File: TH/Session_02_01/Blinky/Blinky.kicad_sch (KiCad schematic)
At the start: 12 parts, among them SW1 SW_SPDT, U1 TLC551CD‎

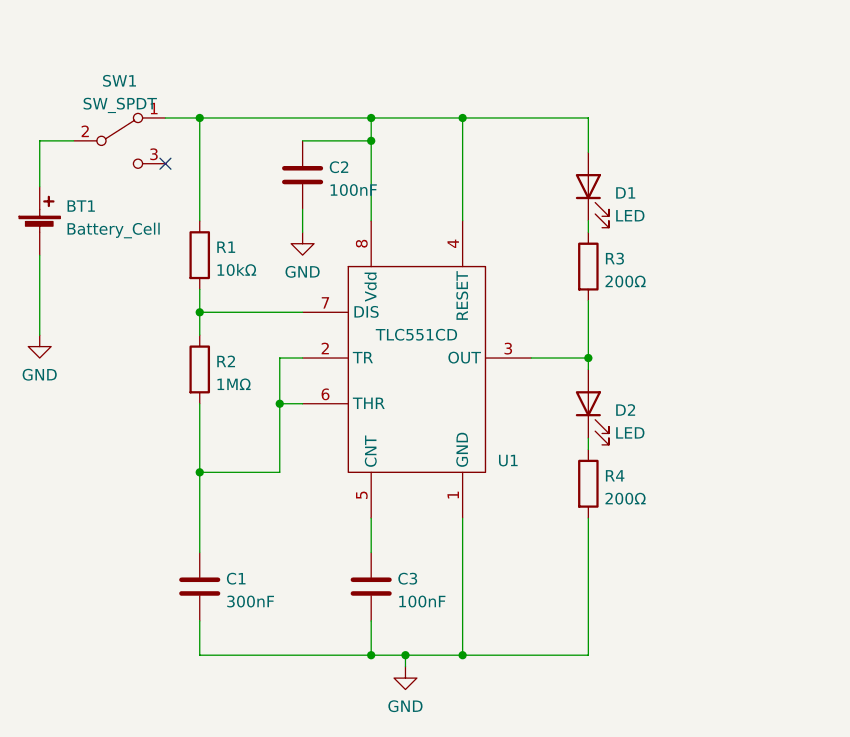
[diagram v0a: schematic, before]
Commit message: Revamps the through-hole project as transistor based
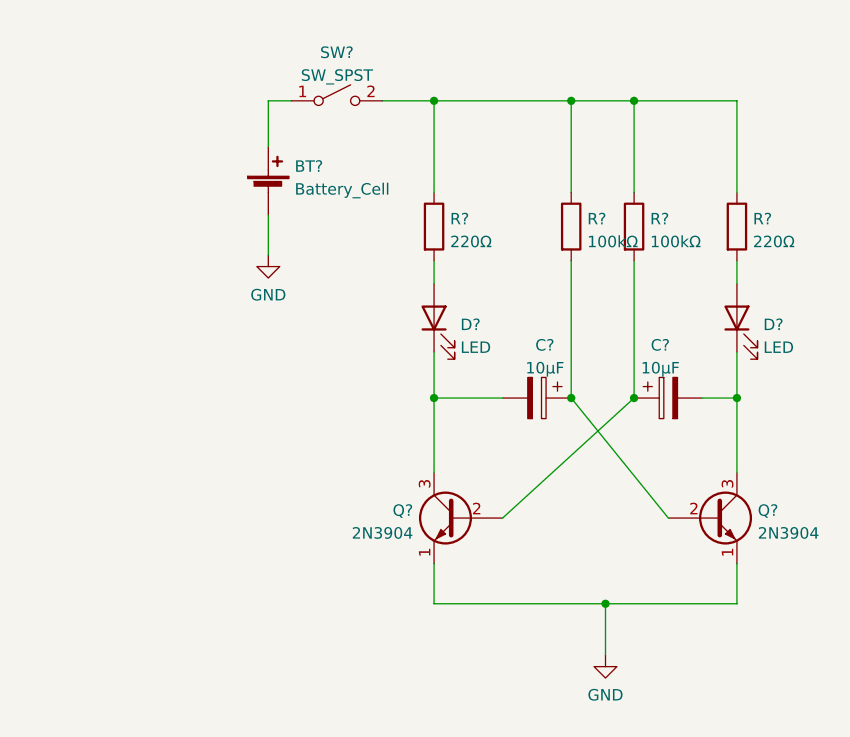
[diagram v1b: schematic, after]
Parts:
- removed BT1: Battery_Cell, Battery:BatteryHolder_Keystone_3000_1x12mm, symbol Device:Battery_Cell
- removed C1: 300nF, Capacitor_THT:C_Disc_D5.0mm_W2.5mm_P5.00mm, symbol Device:C
- removed C2, C3: 100nF, Capacitor_THT:C_Disc_D5.0mm_W2.5mm_P5.00mm, symbol Device:C
- removed D1, D2: LED, LED_THT:LED_D5.0mm, symbol Device:LED
- removed R1: 10kΩ, Resistor_THT:R_Axial_DIN0207_L6.3mm_D2.5mm_P10.16mm_Horizontal, symbol Device:R
- removed R2: 1MΩ, Resistor_THT:R_Axial_DIN0207_L6.3mm_D2.5mm_P10.16mm_Horizontal, symbol Device:R
- removed R3, R4: 200Ω, Resistor_THT:R_Axial_DIN0207_L6.3mm_D2.5mm_P10.16mm_Horizontal, symbol Device:R
- removed SW1: SW_SPDT, Blinky_ZAM:SSK-1202, symbol Switch:SW_SPDT
- removed U1: TLC551CD‎, Package_DIP:DIP-8_W7.62mm_Socket, symbol Blinky:TLC551CD‎
- added BT?: Battery_Cell, Battery:BatteryHolder_Keystone_3000_1x12mm, symbol Device:Battery_Cell
- added C? (x2): 10μF, Capacitor_THT:CP_Radial_D5.0mm_P2.50mm, symbol Device:C_Polarized
- added D? (x2): LED, LED_THT:LED_D5.0mm, symbol Device:LED
- added Q? (x2): 2N3904, Package_TO_SOT_THT:TO-92_Inline, symbol Transistor_BJT:2N3904
- added R? (x2): 220Ω, Resistor_THT:R_Axial_DIN0207_L6.3mm_D2.5mm_P2.54mm_Vertical, symbol Device:R
- added R? (x2): 100kΩ, Resistor_THT:R_Axial_DIN0207_L6.3mm_D2.5mm_P2.54mm_Vertical, symbol Device:R
- added SW?: SW_SPST, Blinky_ZAM:SSK-1202, symbol Switch:SW_SPST
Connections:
- net GND: now also BT?.2 (-), Q?.1 (E), Q?.1 (E)
- new net: C?.2, D?.1 (K), Q?.3 (C) (x2)
- new net: D?.2 (A), R?.2 (x2)
- new net: R?.1, R?.1, R?.1, R?.1, SW?.2 (B)
- new net: C?.1, Q?.2 (B), R?.2 (x2)
- new net: BT?.1 (+), SW?.1 (A)
- no-connect marks 1 -> 0

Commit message: Makes corrections to the design rules
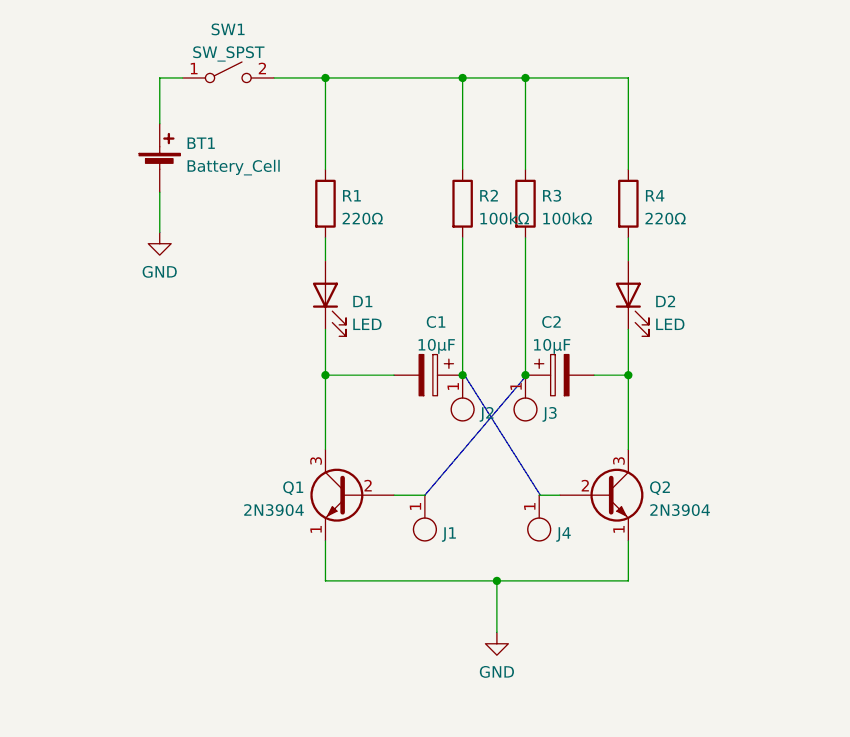
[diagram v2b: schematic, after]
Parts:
- removed BT?: Battery_Cell, Battery:BatteryHolder_Keystone_3000_1x12mm, symbol Device:Battery_Cell
- removed C? (x2): 10μF, Capacitor_THT:CP_Radial_D5.0mm_P2.50mm, symbol Device:C_Polarized
- removed D? (x2): LED, LED_THT:LED_D5.0mm, symbol Device:LED
- removed Q? (x2): 2N3904, Package_TO_SOT_THT:TO-92_Inline, symbol Transistor_BJT:2N3904
- removed R? (x2): 220Ω, Resistor_THT:R_Axial_DIN0207_L6.3mm_D2.5mm_P2.54mm_Vertical, symbol Device:R
- removed R? (x2): 100kΩ, Resistor_THT:R_Axial_DIN0207_L6.3mm_D2.5mm_P2.54mm_Vertical, symbol Device:R
- removed SW?: SW_SPST, Blinky_ZAM:SSK-1202, symbol Switch:SW_SPST
- added BT1: Battery_Cell, Battery:BatteryHolder_Keystone_3000_1x12mm, symbol Device:Battery_Cell
- added C1, C2: 10μF, Capacitor_THT:CP_Radial_D5.0mm_P2.50mm, symbol Device:C_Polarized
- added D1, D2: LED, LED_THT:LED_D5.0mm, symbol Device:LED
- added J1, J2, J3, J4: Jumper_1, TestPoint:TestPoint_THTPad_2.0x2.0mm_Drill1.0mm, symbol Blinky:Jumper_1
- added Q1, Q2: 2N3904, Package_TO_SOT_THT:TO-92_Inline, symbol Transistor_BJT:2N3904
- added R1, R4: 220Ω, Resistor_THT:R_Axial_DIN0207_L6.3mm_D2.5mm_P2.54mm_Vertical, symbol Device:R
- added R2, R3: 100kΩ, Resistor_THT:R_Axial_DIN0207_L6.3mm_D2.5mm_P2.54mm_Vertical, symbol Device:R
- added SW1: SW_SPST, Blinky_ZAM:SSK-1202, symbol Switch:SW_SPST
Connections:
- net GND: now also BT1.2 (-), Q1.1 (E), Q2.1 (E)
- new net: C1.1, J2.1, R2.2
- new net: BT1.1 (+), SW1.1 (A)
- new net: J1.1, Q1.2 (B)
- new net: C1.2, D1.1 (K), Q1.3 (C)
- new net: C2.1, J3.1, R3.2
- new net: C2.2, D2.1 (K), Q2.3 (C)
- new net: R1.1, R2.1, R3.1, R4.1, SW1.2 (B)
- new net: D1.2 (A), R1.2
- new net: J4.1, Q2.2 (B)
- new net: D2.2 (A), R4.2
